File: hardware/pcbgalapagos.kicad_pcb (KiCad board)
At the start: 2 copper layers, 140.5 x 106 mm, 55 parts, among them J1 Battery, U1 ESP32_DevKit, U2 INA226, U3 BME280, U4 LSM6DS, U5 MAX31855, U6 RFM95_Emissor, U7 GPS_NEO, U8 TPS62160DGK, U9 TPS62160DGK

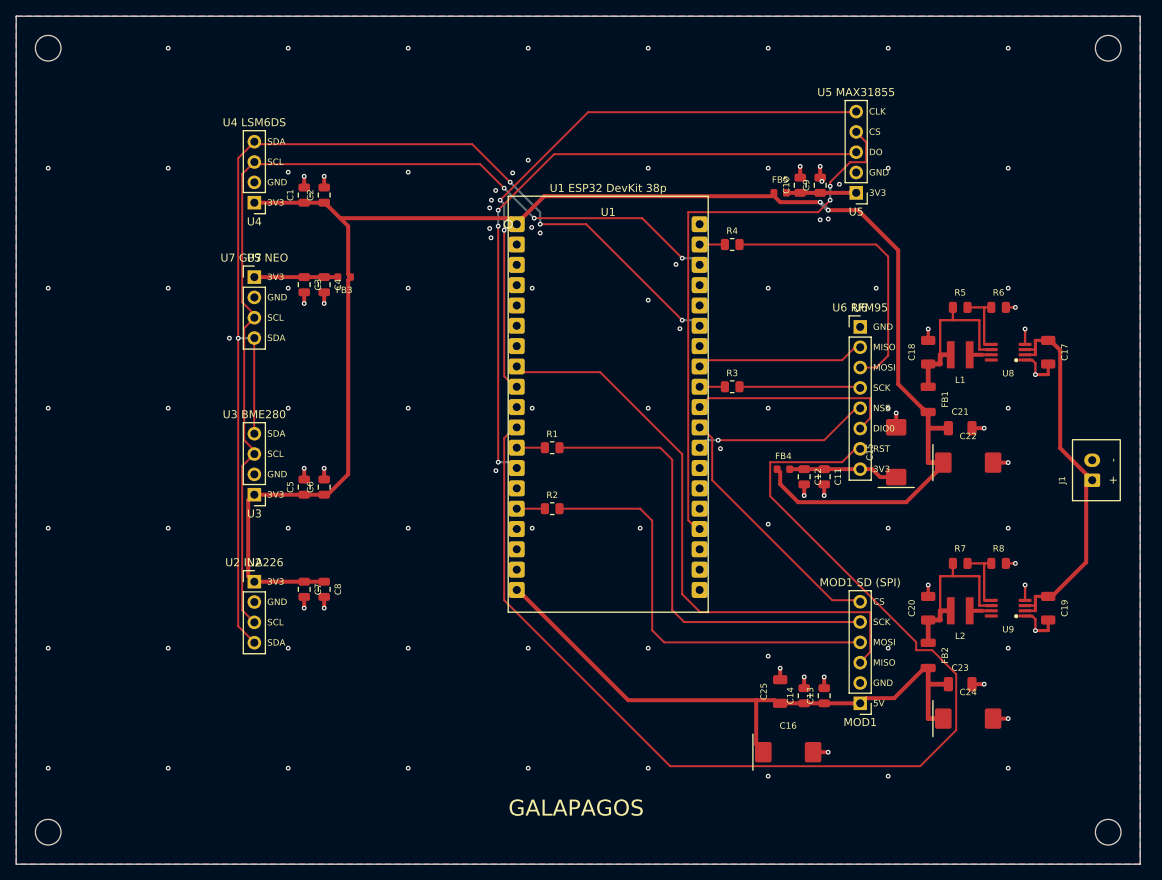
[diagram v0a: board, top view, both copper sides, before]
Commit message: Final PCB, schematic and project libraries
Replace hardware with the final KiCad 10 project: module headers matched
to the real breakouts, GPS UART header, input protection, MISO series
termination, test points, solid SMD pour connections. Add the project
footprint library and fp-lib-table. Drop the outdated BOM and renders.
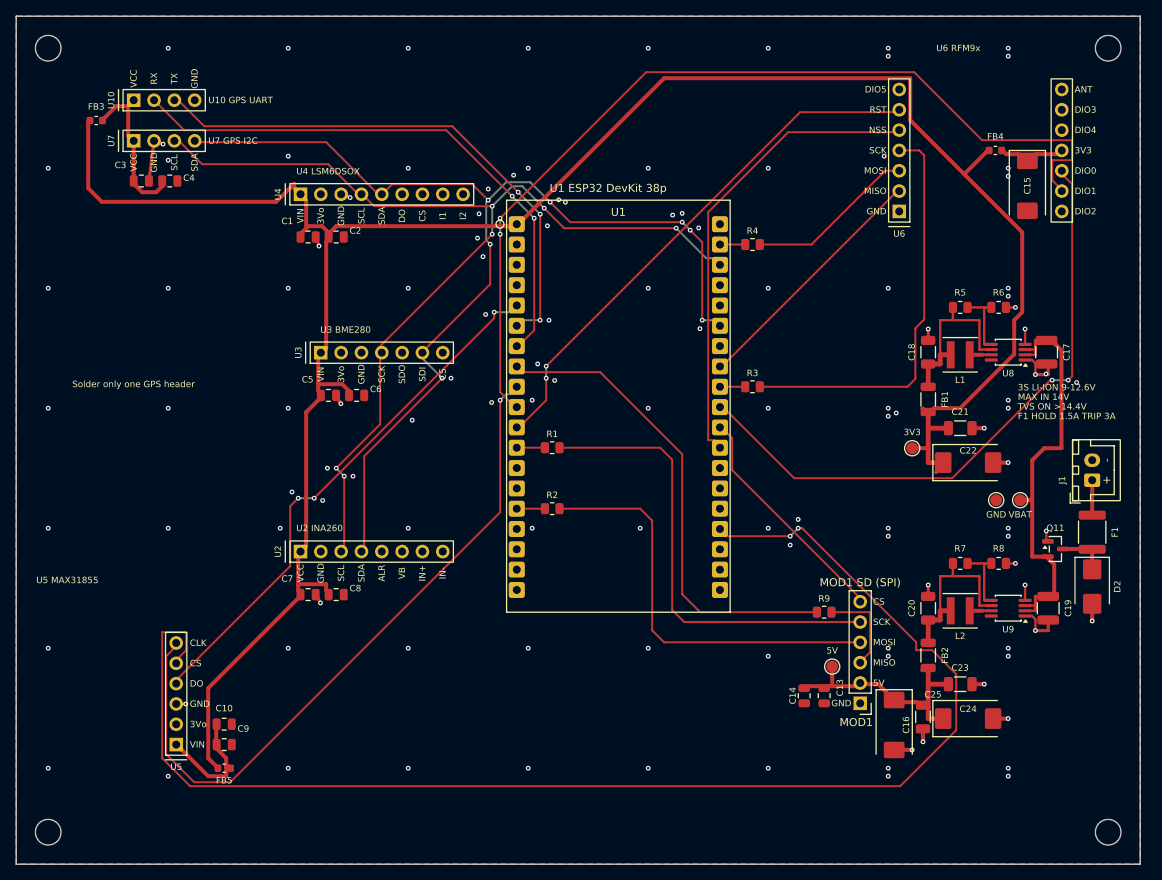
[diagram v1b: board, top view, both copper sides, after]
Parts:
- removed C11: 100nF 50V X7R, Capacitor_SMD:C_0805_2012Metric
- removed C12: 10uF 16V X7R, Capacitor_SMD:C_0805_2012Metric
- added D2: SMBJ13CA, Diode_SMD:D_SMB, F.Cu at (216.5, 117.3)
- added F1: MF-MSMF150/16X-2, Fuse:Fuse_1812_4532Metric, F.Cu at (216.5, 110.5)
- added Q11: DMP3056L-7, Package_TO_SOT_SMD:SOT-23, F.Cu at (211.9, 112.6)
- added R9: 33, Resistor_SMD:R_0805_2012Metric, F.Cu at (183.0, 120.5)
- added TP1: TestPoint, TestPoint:TestPoint_Pad_D1.5mm, F.Cu at (207.5, 106.5)
- added TP2: TestPoint, TestPoint:TestPoint_Pad_D1.5mm, F.Cu at (194.0, 100.0)
- added TP3: TestPoint, TestPoint:TestPoint_Pad_D1.5mm, F.Cu at (184.0, 127.3)
- added TP4: TestPoint, TestPoint:TestPoint_Pad_D1.5mm, F.Cu at (204.5, 106.5)
- added U10: GPS_NEO8M_UART, galapagos_fp:GPS_NEO8M_UART_Header_1x04, F.Cu at (96.7, 56.5)
- C17, C19: value 10uF 25V X7R -> 10uF 50V X7R; footprint Capacitor_SMD:C_1206_3216Metric -> Capacitor_SMD:C_1210_3225Metric
- U1: footprint ESP32_Custom:ESP32_38Pin -> galapagos_fp:ESP32_DevKitC_V4_38
- U2: value INA226 -> INA260; footprint Connector_PinHeader_2.54mm:PinHeader_1x04_P2.54mm_Vertical -> galapagos_fp:Adafruit_INA260_Header
- U3: footprint Connector_PinHeader_2.54mm:PinHeader_1x04_P2.54mm_Vertical -> galapagos_fp:Adafruit_BME280_Header
- U4: value LSM6DS -> LSM6DSOX; footprint Connector_PinHeader_2.54mm:PinHeader_1x04_P2.54mm_Vertical -> galapagos_fp:Adafruit_LSM6DSOX_Header
- U5: footprint Connector_PinHeader_2.54mm:PinHeader_1x05_P2.54mm_Vertical -> galapagos_fp:Adafruit_MAX31855_Header
- U6: footprint Connector_PinHeader_2.54mm:PinHeader_1x08_P2.54mm_Vertical -> galapagos_fp:RFM9x_Breakout_attexx
- U7: footprint Connector_PinHeader_2.54mm:PinHeader_1x04_P2.54mm_Vertical -> galapagos_fp:GPS_I2C_Header_1x04
- moved U5 109.5 mm to (102.0, 137.1)
- moved C9 102.2 mm to (108.0, 137.1), turned to 0 degrees
- moved FB5 100.0 mm to (108.0, 140.0)
- moved C10 98.6 mm to (108.0, 134.5), turned to 0 degrees
- moved FB4 47.8 mm to (204.4, 62.8)
- moved C15 37.1 mm to (208.4, 67.2), turned to -90 degrees
- moved FB3 36.7 mm to (92.0, 59.0), turned to 0 degrees
- moved C3 24.1 mm to (97.6, 66.6), turned to 0 degrees
- moved C4 23.2 mm to (101.2, 66.6), turned to 0 degrees
- moved U7 22.7 mm to (96.7, 61.6), turned to 90 degrees
- moved U3 19.6 mm to (120.1, 88.1), turned to 90 degrees
- moved C25 18.1 mm to (195.3, 133.6), turned to -90 degrees
- moved U6 15.2 mm to (192.4, 70.4), turned to 180 degrees
- moved C16 13.7 mm to (191.8, 134.6), turned to -90 degrees
- moved C6 12.2 mm to (124.5, 93.4), turned to 0 degrees
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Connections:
- J1 pad 1: VBAT -> VBAT_IN
- MOD1 pad 1: +5V -> GND
- MOD1 pad 2: GND -> +5V
- MOD1 pad 3: HSPI_MISO -> HSPI_MISO_SD
- U1 pad 10: (no net) -> RFM_DIO1
- U1 pad 13: MAX_DO -> (no net)
- U1 pad 19: +5V -> (no net)
- U1 pad 5: (no net) -> MAX_DO
- U1 pad 6: (no net) -> GPS_TXD
- U1 pad 7: (no net) -> GPS_RXD
- U3 pad 2: GND -> (no net)
- U3 pad 3: I2C_SCL -> GND
- U3 pad 4: I2C_SDA -> I2C_SCL
- U4 pad 2: GND -> (no net)
- U4 pad 3: I2C_SCL -> GND
- U4 pad 4: I2C_SDA -> I2C_SCL
- U5 pad 2: GND -> (no net)
- U5 pad 3: MAX_DO -> GND
- U5 pad 4: MAX_CS -> MAX_DO
- U5 pad 5: MAX_CLK -> MAX_CS
- U6 pad 6: RFM_DIO0 -> RFM_RST
- U6 pad 7: RFM_RST -> (no net)
- U6 pad 8: +3V3_RF -> (no net)
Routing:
- net RFM_DIO1: track 0.00 -> 116.4 mm, vias 0 -> 2
- net MAX_CS: track 70.8 -> 172.2 mm
- net RFM_RST: track 145.5 -> 66.6 mm, vias 0 -> 2
- net +3V3: track 210.3 -> 285.0 mm, vias 2 -> 0
- net GPS_RXD: track 0.00 -> 70.6 mm, vias 0 -> 2
- net GPS_TXD: track 0.00 -> 68.0 mm, vias 0 -> 3
- net RFM_DIO0: track 26.1 -> 79.1 mm, vias 0 -> 2
- net +5V: track 76.5 -> 30.1 mm
- net VSPI_SCK: track 15.1 -> 51.6 mm
- net VSPI_CS_RFM: track 22.1 -> 58.5 mm, vias 1 -> 0
- net MAX_CLK: track 73.3 -> 88.3 mm, vias 2 -> 1
- net MAX_DO: track 81.8 -> 67.2 mm
- net VSPI_MOSI: track 35.7 -> 21.2 mm
- net HSPI_MISO: track 73.9 -> 60.4 mm
- net HSPI_MISO_SD: track 0.00 -> 11.6 mm
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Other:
- board text added: "3S LI-ION 9-12.6V"
- board text added: "3Vo"
- board text added: "ALR"
- board text added: "ANT"
- board text added: "DIO1"
- board text added: "DIO2"
- board text added: "DIO3"
- board text added: "DIO4"
- board text added: "DIO5"
- board text added: "F1 HOLD 1.5A TRIP 3A"
- board text added: "I1"
- board text added: "I2"
- board text added: "IN+"
- board text added: "IN-"
- board text added: "MAX IN 14V"
- board text added: "RX"
- board text added: "SDI"
- board text added: "SDO"
- board text added: "Solder only one GPS header"
- board text added: "TVS ON >14.4V"
- board text added: "TX"
- board text added: "U10 GPS UART"
- board text added: "U2 INA260"
- board text added: "U4 LSM6DSOX"
- board text added: "U6 RFM9x"
- board text added: "U7 GPS I2C"
- board text added: "VB"
- board text added: "VBAT"
- board text added: "VCC"
- board text added: "VIN"
- board text removed: "GALAPAGOS"
- board text removed: "U2 INA226"
- board text removed: "U4 LSM6DS"
- board text removed: "U6 RFM95"
- board text removed: "U7 GPS NEO"
